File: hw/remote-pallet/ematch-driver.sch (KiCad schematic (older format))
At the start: 8 parts

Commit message: really commiting changes to the schematic this time
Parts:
- removed D?: ZENER, symbol ZENER
- R10: renamed from R?; value R -> 500
- R11, R12: renamed from R?; value R -> 10k
- gave numbers to parts that had none: 4
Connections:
- net GPIO_IN_SENSE is gone; now on net EMATCH_GND: R10.2
- net EMATCH_VCC: no longer D1.1 (K)
- net VSENSE: now reaches D2.2 (A), R10.1
- net VSENSE: now also D1.1 (K)
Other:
- moved on the sheet: D14
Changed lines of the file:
@@
 LIBS:contrib
 LIBS:valves
+LIBS:iot_photon_headers
 LIBS:remote-pallet-cache
 EELAYER 25 0
@@
 $Descr A4 11693 8268
 encoding utf-8
-Sheet 4 4
+Sheet 8 9
 Title ""
 Date ""
@@
 $EndDescr
 $Comp
-L R R?
+L R R10
 U 1 1 56CFCF8E
 P 3000 4100
-AR Path="/56CFDAEF/56CFCF8E" Ref="R?"  Part="1"
-AR Path="/56D11458/56CFCF8E" Ref="R?"  Part="1"
-F 0 "R?" V 3080 4100 50  0000 C CNN
-F 1 "R" V 3000 4100 50  0000 C CNN
+AR Path="/56CFDAEF/56CFCF8E" Ref="R10"  Part="1"
+AR Path="/56D11458/56CFCF8E" Ref="R16"  Part="1"
+AR Path="/56D0EADF/56CFCF8E" Ref="R13"  Part="1"
+AR Path="/56EA4F7F/56CFCF8E" Ref="R19"  Part="1"
+AR Path="/56EAA678/56CFCF8E" Ref="R22"  Part="1"
+AR Path="/56EAA681/56CFCF8E" Ref="R25"  Part="1"
+AR Path="/56EAA68A/56CFCF8E" Ref="R28"  Part="1"
+AR Path="/56EAA6CF/56CFCF8E" Ref="R31"  Part="1"
+F 0 "R28" V 3080 4100 50  0000 C CNN
+F 1 "500" V 3000 4100 50  0000 C CNN
 F 2 "" V 2930 4100 50  0000 C CNN
 F 3 "" H 3000 4100 50  0000 C CNN
@@
 $EndComp
 $Comp
-L R R?
+L R R11
 U 1 1 56CFD0B3
 P 3050 2600
-AR Path="/56CFDAEF/56CFD0B3" Ref="R?"  Part="1"
-AR Path="/56D11458/56CFD0B3" Ref="R?"  Part="1"
-F 0 "R?" V 3130 2600 50  0000 C CNN
-F 1 "R" V 3050 2600 50  0000 C CNN
+AR Path="/56CFDAEF/56CFD0B3" Ref="R11"  Part="1"
+AR Path="/56D11458/56CFD0B3" Ref="R17"  Part="1"
+AR Path="/56D0EADF/56CFD0B3" Ref="R14"  Part="1"
+AR Path="/56EA4F7F/56CFD0B3" Ref="R20"  Part="1"
+AR Path="/56EAA678/56CFD0B3" Ref="R23"  Part="1"
+AR Path="/56EAA681/56CFD0B3" Ref="R26"  Part="1"
+AR Path="/56EAA68A/56CFD0B3" Ref="R29"  Part="1"
+AR Path="/56EAA6CF/56CFD0B3" Ref="R32"  Part="1"
+F 0 "R29" V 3130 2600 50  0000 C CNN
+F 1 "10k" V 3050 2600 50  0000 C CNN
 F 2 "" V 2980 2600 50  0000 C CNN
 F 3 "" H 3050 2600 50  0000 C CNN
@@
 $EndComp
 $Comp
-L Q_NMOS_DGS Q?
+L Q_NMOS_DGS Q3
 U 1 1 56CFD248
 P 4000 1750
-AR Path="/56CFDAEF/56CFD248" Ref="Q?"  Part="1"
-AR Path="/56D11458/56CFD248" Ref="Q?"  Part="1"
-F 0 "Q?" H 4300 1800 50  0000 R CNN
+AR Path="/56CFDAEF/56CFD248" Ref="Q3"  Part="1"
+AR Path="/56D11458/56CFD248" Ref="Q7"  Part="1"
+AR Path="/56D0EADF/56CFD248" Ref="Q5"  Part="1"
+AR Path="/56EA4F7F/56CFD248" Ref="Q9"  Part="1"
+AR Path="/56EAA678/56CFD248" Ref="Q11"  Part="1"
+AR Path="/56EAA681/56CFD248" Ref="Q13"  Part="1"
+AR Path="/56EAA68A/56CFD248" Ref="Q15"  Part="1"
+AR Path="/56EAA6CF/56CFD248" Ref="Q17"  Part="1"
+F 0 "Q15" H 4300 1800 50  0000 R CNN
 F 1 "Q_NMOS_DGS" H 4650 1700 50  0000 R CNN
 F 2 "" H 4200 1850 50  0000 C CNN
@@
 $EndComp
 $Comp
-L Q_PMOS_DGS Q?
+L Q_PMOS_DGS Q2
 U 1 1 56CFDBA4
 P 3450 2100
-AR Path="/56CFDAEF/56CFDBA4" Ref="Q?"  Part="1"
-AR Path="/56D11458/56CFDBA4" Ref="Q?"  Part="1"
-F 0 "Q?" H 3750 2150 50  0000 R CNN
+AR Path="/56CFDAEF/56CFDBA4" Ref="Q2"  Part="1"
+AR Path="/56D11458/56CFDBA4" Ref="Q6"  Part="1"
+AR Path="/56D0EADF/56CFDBA4" Ref="Q4"  Part="1"
+AR Path="/56EA4F7F/56CFDBA4" Ref="Q8"  Part="1"
+AR Path="/56EAA678/56CFDBA4" Ref="Q10"  Part="1"
+AR Path="/56EAA681/56CFDBA4" Ref="Q12"  Part="1"
+AR Path="/56EAA68A/56CFDBA4" Ref="Q14"  Part="1"
+AR Path="/56EAA6CF/56CFDBA4" Ref="Q16"  Part="1"
+F 0 "Q14" H 3750 2150 50  0000 R CNN
 F 1 "Q_PMOS_DGS" H 4100 2050 50  0000 R CNN
 F 2 "" H 3650 2200 50  0000 C CNN
@@
 $EndComp
 $Comp
-L R R?
+L R R12
 U 1 1 56CFDBE5
 P 3550 1400
-AR Path="/56CFDAEF/56CFDBE5" Ref="R?"  Part="1"
-AR Path="/56D11458/56CFDBE5" Ref="R?"  Part="1"
-F 0 "R?" V 3630 1400 50  0000 C CNN
-F 1 "R" V 3550 1400 50  0000 C CNN
+AR Path="/56CFDAEF/56CFDBE5" Ref="R12"  Part="1"
+AR Path="/56D11458/56CFDBE5" Ref="R18"  Part="1"
+AR Path="/56D0EADF/56CFDBE5" Ref="R15"  Part="1"
+AR Path="/56EA4F7F/56CFDBE5" Ref="R21"  Part="1"
+AR Path="/56EAA678/56CFDBE5" Ref="R24"  Part="1"
+AR Path="/56EAA681/56CFDBE5" Ref="R27"  Part="1"
+AR Path="/56EAA68A/56CFDBE5" Ref="R30"  Part="1"
+AR Path="/56EAA6CF/56CFDBE5" Ref="R33"  Part="1"
+F 0 "R30" V 3630 1400 50  0000 C CNN
+F 1 "10k" V 3550 1400 50  0000 C CNN
 F 2 "" V 3480 1400 50  0000 C CNN
 F 3 "" H 3550 1400 50  0000 C CNN
@@
 $EndComp
 $Comp
-L D D?
+L D D2
 U 1 1 56CFDC9F
-P 3550 4100
-AR Path="/56CFDAEF/56CFDC9F" Ref="D?"  Part="1"
-AR Path="/56D11458/56CFDC9F" Ref="D?"  Part="1"
-F 0 "D?" H 3550 4200 50  0000 C CNN
-F 1 "D" H 3550 4000 50  0000 C CNN
-F 2 "" H 3550 4100 50  0000 C CNN
-F 3 "" H 3550 4100 50  0000 C CNN
-	1    3550 4100
+P 3900 4650
+AR Path="/56CFDAEF/56CFDC9F" Ref="D2"  Part="1"
+AR Path="/56D11458/56CFDC9F" Ref="D6"  Part="1"
+AR Path="/56D0EADF/56CFDC9F" Ref="D4"  Part="1"
+AR Path="/56EA4F7F/56CFDC9F" Ref="D8"  Part="1"
+AR Path="/56EAA678/56CFDC9F" Ref="D10"  Part="1"
+AR Path="/56EAA681/56CFDC9F" Ref="D12"  Part="1"
+AR Path="/56EAA68A/56CFDC9F" Ref="D14"  Part="1"
+AR Path="/56EAA6CF/56CFDC9F" Ref="D16"  Part="1"
+F 0 "D14" H 3900 4750 50  0000 C CNN
+F 1 "D" H 3900 4550 50  0000 C CNN
+F 2 "" H 3900 4650 50  0000 C CNN
+F 3 "" H 3900 4650 50  0000 C CNN
+	1    3900 4650
 	-1   0    0    -1
 $EndComp
 $Comp
-L ZENER D?
+L ZENER D1
 U 1 1 56CFDD3A
 P 3550 5100
-AR Path="/56CFDAEF/56CFDD3A" Ref="D?"  Part="1"
-AR Path="/56D11458/56CFDD3A" Ref="D?"  Part="1"
-F 0 "D?" H 3550 5200 50  0000 C CNN
+AR Path="/56CFDAEF/56CFDD3A" Ref="D1"  Part="1"
+AR Path="/56D11458/56CFDD3A" Ref="D5"  Part="1"
+AR Path="/56D0EADF/56CFDD3A" Ref="D3"  Part="1"
+AR Path="/56EA4F7F/56CFDD3A" Ref="D7"  Part="1"
+AR Path="/56EAA678/56CFDD3A" Ref="D9"  Part="1"
+AR Path="/56EAA681/56CFDD3A" Ref="D11"  Part="1"
+AR Path="/56EAA68A/56CFDD3A" Ref="D13"  Part="1"
+AR Path="/56EAA6CF/56CFDD3A" Ref="D15"  Part="1"
+F 0 "D13" H 3550 5200 50  0000 C CNN
 F 1 "ZENER" H 3550 5000 50  0000 C CNN
 F 2 "" H 3550 5100 50  0000 C CNN
@@
 	0    1    1    0
 $EndComp
-$Comp
-L ZENER D?
-U 1 1 56CFDDAF
-P 2500 4550
-AR Path="/56CFDAEF/56CFDDAF" Ref="D?"  Part="1"
-AR Path="/56D11458/56CFDDAF" Ref="D?"  Part="1"
-F 0 "D?" H 2500 4650 50  0000 C CNN
-F 1 "ZENER" H 2500 4450 50  0000 C CNN
-F 2 "" H 2500 4550 50  0000 C CNN
-F 3 "" H 2500 4550 50  0000 C CNN
-	1    2500 4550
-	0    1    1    0
-$EndComp
 Wire Wire Line
 	3850 850  3850 1100
@@
 	4100 1950 4100 5000
 Wire Wire Line
-	2500 4350 2500 4100
+	2500 4100 2500 5000
 Wire Wire Line
 	2050 4100 2850 4100
 Wire Wire Line
-	3150 4100 3400 4100
-Wire Wire Line
-	3700 4100 4100 4100
+	3150 4100 3550 4100
 Connection ~ 4100 4100
 Wire Wire Line
@@
 Wire Wire Line
 	4100 5300 4100 5750
-Wire Wire Line
-	2500 4750 2500 5000
 Connection ~ 2500 4100
 Wire Wire Line
-	3550 4650 3550 4900
+	3550 4100 3550 4900
 Connection ~ 4100 4650
 Connection ~ 3550 4650
 Wire Wire Line
 	3550 5300 3550 5500
-Wire Wire Line
-	3400 4650 4100 4650
 Connection ~ 3050 2100
 Text HLabel 2050 4100 0    60   Input ~ 0
@@
 Text HLabel 4100 5750 3    60   Input ~ 0
 GND
+Wire Wire Line
+	4100 4650 4050 4650
+Wire Wire Line
+	3400 4650 3750 4650
 $EndSCHEMATC

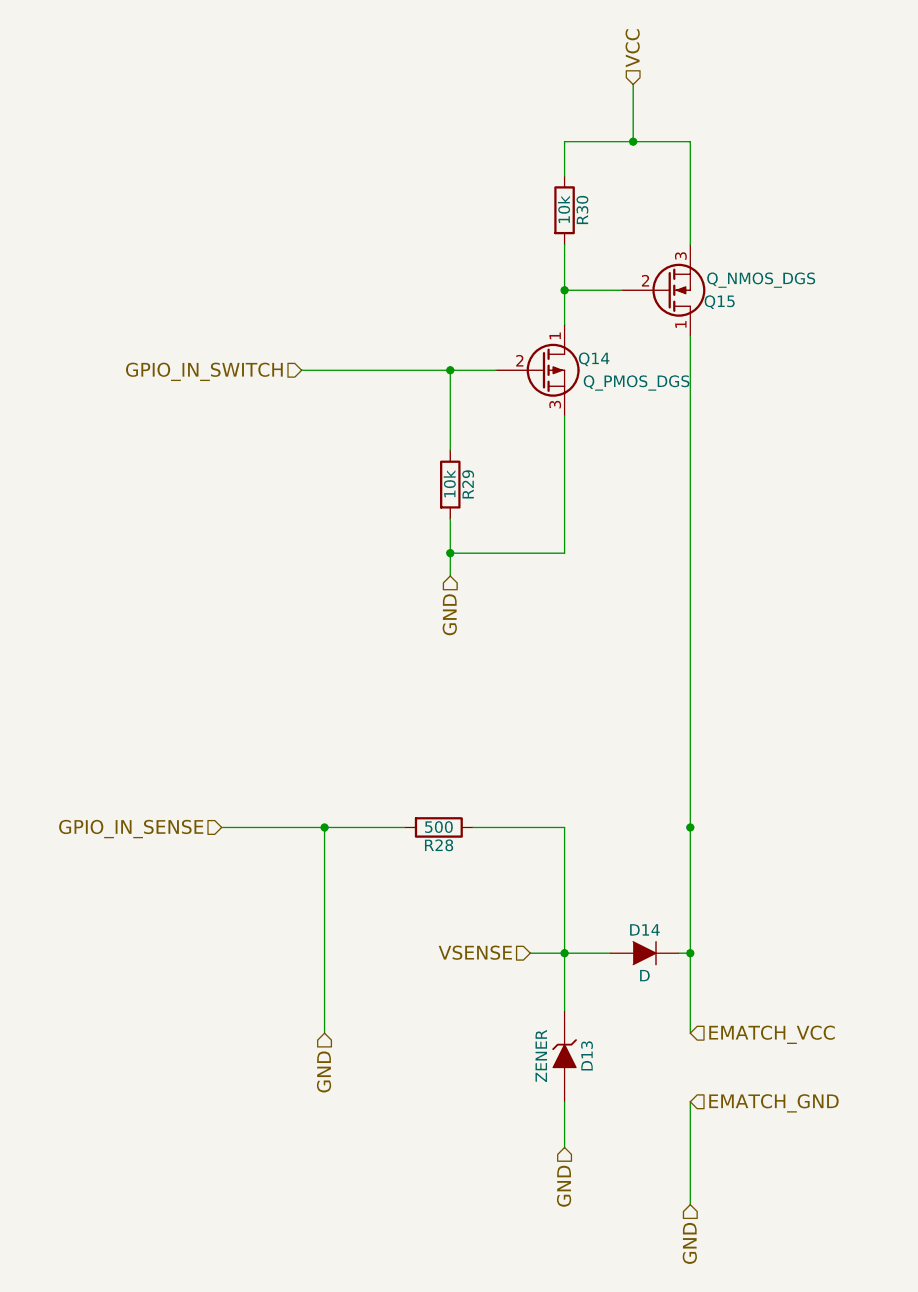
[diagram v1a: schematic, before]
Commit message: adding second switch
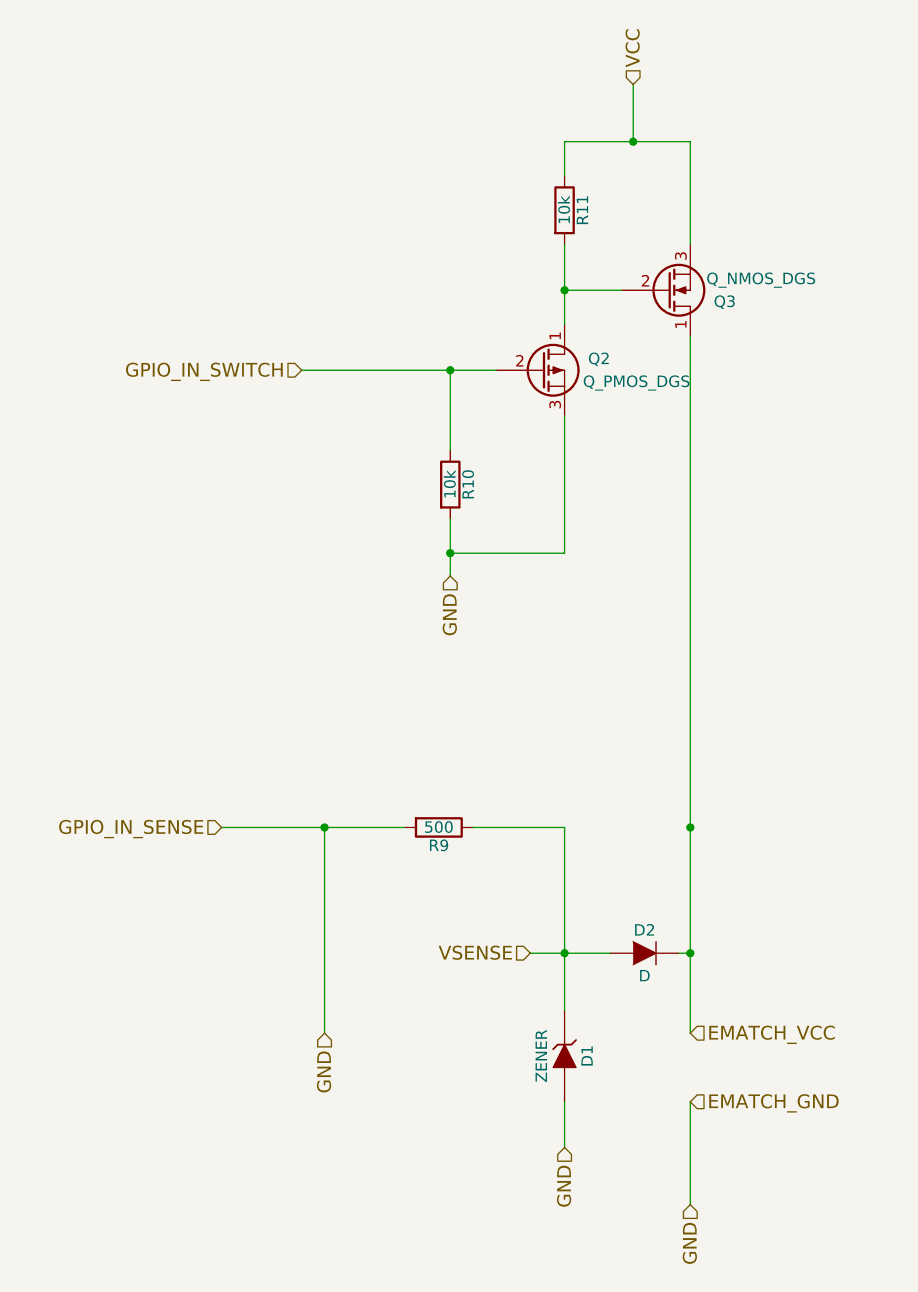
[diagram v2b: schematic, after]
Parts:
- renumbered R11 to R10, R12 to R11, R10 to R9
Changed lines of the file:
@@
 $Descr A4 11693 8268
 encoding utf-8
-Sheet 8 9
+Sheet 2 9
 Title ""
 Date ""
@@
 $EndDescr
 $Comp
-L R R10
+L R R9
 U 1 1 56CFCF8E
 P 3000 4100
-AR Path="/56CFDAEF/56CFCF8E" Ref="R10"  Part="1"
-AR Path="/56D11458/56CFCF8E" Ref="R16"  Part="1"
-AR Path="/56D0EADF/56CFCF8E" Ref="R13"  Part="1"
-AR Path="/56EA4F7F/56CFCF8E" Ref="R19"  Part="1"
-AR Path="/56EAA678/56CFCF8E" Ref="R22"  Part="1"
-AR Path="/56EAA681/56CFCF8E" Ref="R25"  Part="1"
-AR Path="/56EAA68A/56CFCF8E" Ref="R28"  Part="1"
-AR Path="/56EAA6CF/56CFCF8E" Ref="R31"  Part="1"
-F 0 "R28" V 3080 4100 50  0000 C CNN
+AR Path="/56CFDAEF/56CFCF8E" Ref="R9"  Part="1"
+AR Path="/56D0EADF/56CFCF8E" Ref="R12"  Part="1"
+AR Path="/56D11458/56CFCF8E" Ref="R15"  Part="1"
+AR Path="/56EA4F7F/56CFCF8E" Ref="R18"  Part="1"
+AR Path="/56EAA678/56CFCF8E" Ref="R21"  Part="1"
+AR Path="/56EAA681/56CFCF8E" Ref="R24"  Part="1"
+AR Path="/56EAA68A/56CFCF8E" Ref="R27"  Part="1"
+AR Path="/56EAA6CF/56CFCF8E" Ref="R30"  Part="1"
+F 0 "R9" V 3080 4100 50  0000 C CNN
 F 1 "500" V 3000 4100 50  0000 C CNN
 F 2 "" V 2930 4100 50  0000 C CNN
@@
 $EndComp
 $Comp
-L R R11
+L R R10
 U 1 1 56CFD0B3
 P 3050 2600
-AR Path="/56CFDAEF/56CFD0B3" Ref="R11"  Part="1"
-AR Path="/56D11458/56CFD0B3" Ref="R17"  Part="1"
-AR Path="/56D0EADF/56CFD0B3" Ref="R14"  Part="1"
-AR Path="/56EA4F7F/56CFD0B3" Ref="R20"  Part="1"
-AR Path="/56EAA678/56CFD0B3" Ref="R23"  Part="1"
-AR Path="/56EAA681/56CFD0B3" Ref="R26"  Part="1"
-AR Path="/56EAA68A/56CFD0B3" Ref="R29"  Part="1"
-AR Path="/56EAA6CF/56CFD0B3" Ref="R32"  Part="1"
-F 0 "R29" V 3130 2600 50  0000 C CNN
+AR Path="/56CFDAEF/56CFD0B3" Ref="R10"  Part="1"
+AR Path="/56D0EADF/56CFD0B3" Ref="R13"  Part="1"
+AR Path="/56D11458/56CFD0B3" Ref="R16"  Part="1"
+AR Path="/56EA4F7F/56CFD0B3" Ref="R19"  Part="1"
+AR Path="/56EAA678/56CFD0B3" Ref="R22"  Part="1"
+AR Path="/56EAA681/56CFD0B3" Ref="R25"  Part="1"
+AR Path="/56EAA68A/56CFD0B3" Ref="R28"  Part="1"
+AR Path="/56EAA6CF/56CFD0B3" Ref="R31"  Part="1"
+F 0 "R10" V 3130 2600 50  0000 C CNN
 F 1 "10k" V 3050 2600 50  0000 C CNN
 F 2 "" V 2980 2600 50  0000 C CNN
@@
 P 4000 1750
 AR Path="/56CFDAEF/56CFD248" Ref="Q3"  Part="1"
+AR Path="/56D0EADF/56CFD248" Ref="Q5"  Part="1"
 AR Path="/56D11458/56CFD248" Ref="Q7"  Part="1"
-AR Path="/56D0EADF/56CFD248" Ref="Q5"  Part="1"
 AR Path="/56EA4F7F/56CFD248" Ref="Q9"  Part="1"
 AR Path="/56EAA678/56CFD248" Ref="Q11"  Part="1"
@@
 AR Path="/56EAA68A/56CFD248" Ref="Q15"  Part="1"
 AR Path="/56EAA6CF/56CFD248" Ref="Q17"  Part="1"
-F 0 "Q15" H 4300 1800 50  0000 R CNN
+F 0 "Q3" H 4300 1800 50  0000 R CNN
 F 1 "Q_NMOS_DGS" H 4650 1700 50  0000 R CNN
 F 2 "" H 4200 1850 50  0000 C CNN
@@
 P 3450 2100
 AR Path="/56CFDAEF/56CFDBA4" Ref="Q2"  Part="1"
+AR Path="/56D0EADF/56CFDBA4" Ref="Q4"  Part="1"
 AR Path="/56D11458/56CFDBA4" Ref="Q6"  Part="1"
-AR Path="/56D0EADF/56CFDBA4" Ref="Q4"  Part="1"
 AR Path="/56EA4F7F/56CFDBA4" Ref="Q8"  Part="1"
 AR Path="/56EAA678/56CFDBA4" Ref="Q10"  Part="1"
@@
 AR Path="/56EAA68A/56CFDBA4" Ref="Q14"  Part="1"
 AR Path="/56EAA6CF/56CFDBA4" Ref="Q16"  Part="1"
-F 0 "Q14" H 3750 2150 50  0000 R CNN
+F 0 "Q2" H 3750 2150 50  0000 R CNN
 F 1 "Q_PMOS_DGS" H 4100 2050 50  0000 R CNN
 F 2 "" H 3650 2200 50  0000 C CNN
@@
 $EndComp
 $Comp
-L R R12
+L R R11
 U 1 1 56CFDBE5
 P 3550 1400
-AR Path="/56CFDAEF/56CFDBE5" Ref="R12"  Part="1"
-AR Path="/56D11458/56CFDBE5" Ref="R18"  Part="1"
-AR Path="/56D0EADF/56CFDBE5" Ref="R15"  Part="1"
-AR Path="/56EA4F7F/56CFDBE5" Ref="R21"  Part="1"
-AR Path="/56EAA678/56CFDBE5" Ref="R24"  Part="1"
-AR Path="/56EAA681/56CFDBE5" Ref="R27"  Part="1"
-AR Path="/56EAA68A/56CFDBE5" Ref="R30"  Part="1"
-AR Path="/56EAA6CF/56CFDBE5" Ref="R33"  Part="1"
-F 0 "R30" V 3630 1400 50  0000 C CNN
+AR Path="/56CFDAEF/56CFDBE5" Ref="R11"  Part="1"
+AR Path="/56D0EADF/56CFDBE5" Ref="R14"  Part="1"
+AR Path="/56D11458/56CFDBE5" Ref="R17"  Part="1"
+AR Path="/56EA4F7F/56CFDBE5" Ref="R20"  Part="1"
+AR Path="/56EAA678/56CFDBE5" Ref="R23"  Part="1"
+AR Path="/56EAA681/56CFDBE5" Ref="R26"  Part="1"
+AR Path="/56EAA68A/56CFDBE5" Ref="R29"  Part="1"
+AR Path="/56EAA6CF/56CFDBE5" Ref="R32"  Part="1"
+F 0 "R11" V 3630 1400 50  0000 C CNN
 F 1 "10k" V 3550 1400 50  0000 C CNN
 F 2 "" V 3480 1400 50  0000 C CNN
@@
 P 3900 4650
 AR Path="/56CFDAEF/56CFDC9F" Ref="D2"  Part="1"
+AR Path="/56D0EADF/56CFDC9F" Ref="D4"  Part="1"
 AR Path="/56D11458/56CFDC9F" Ref="D6"  Part="1"
-AR Path="/56D0EADF/56CFDC9F" Ref="D4"  Part="1"
 AR Path="/56EA4F7F/56CFDC9F" Ref="D8"  Part="1"
 AR Path="/56EAA678/56CFDC9F" Ref="D10"  Part="1"
@@
 AR Path="/56EAA68A/56CFDC9F" Ref="D14"  Part="1"
 AR Path="/56EAA6CF/56CFDC9F" Ref="D16"  Part="1"
-F 0 "D14" H 3900 4750 50  0000 C CNN
+F 0 "D2" H 3900 4750 50  0000 C CNN
 F 1 "D" H 3900 4550 50  0000 C CNN
 F 2 "" H 3900 4650 50  0000 C CNN
@@
 P 3550 5100
 AR Path="/56CFDAEF/56CFDD3A" Ref="D1"  Part="1"
+AR Path="/56D0EADF/56CFDD3A" Ref="D3"  Part="1"
 AR Path="/56D11458/56CFDD3A" Ref="D5"  Part="1"
-AR Path="/56D0EADF/56CFDD3A" Ref="D3"  Part="1"
 AR Path="/56EA4F7F/56CFDD3A" Ref="D7"  Part="1"
 AR Path="/56EAA678/56CFDD3A" Ref="D9"  Part="1"
@@
 AR Path="/56EAA68A/56CFDD3A" Ref="D13"  Part="1"
 AR Path="/56EAA6CF/56CFDD3A" Ref="D15"  Part="1"
-F 0 "D13" H 3550 5200 50  0000 C CNN
+F 0 "D1" H 3550 5200 50  0000 C CNN
 F 1 "ZENER" H 3550 5000 50  0000 C CNN
 F 2 "" H 3550 5100 50  0000 C CNN
